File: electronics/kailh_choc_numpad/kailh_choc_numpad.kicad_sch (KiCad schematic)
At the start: 18 parts

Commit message: placed keycaps
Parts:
- cap16, cap17: footprint SquantorSwitches:KAILH_choc_keycap_2 -> SquantorSwitches:KAILH_choc_keycap_2_vertical
- cap5: footprint SquantorSwitches:KAILH_choc_keycap_2 -> SquantorSwitches:KAILH_choc_keycap_2_horizontal
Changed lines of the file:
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@@
       (effects (font (size 1.27 1.27)) (justify left))
     )
-    (property "Footprint" "SquantorSwitches:KAILH_choc_keycap_2" (id 2) (at 279.4 156.21 0)
+    (property "Footprint" "SquantorSwitches:KAILH_choc_keycap_2_vertical" (id 2) (at 279.4 156.21 0)
       (effects (font (size 1.27 1.27)) hide)
     )
@@
       (effects (font (size 1.27 1.27)) (justify left))
     )
-    (property "Footprint" "SquantorSwitches:KAILH_choc_keycap_2" (id 2) (at 264.16 156.21 0)
+    (property "Footprint" "SquantorSwitches:KAILH_choc_keycap_2_horizontal" (id 2) (at 264.16 156.21 0)
       (effects (font (size 1.27 1.27)) hide)
     )
@@
       (effects (font (size 1.27 1.27)) (justify left))
     )
-    (property "Footprint" "SquantorSwitches:KAILH_choc_keycap_2" (id 2) (at 279.4 146.05 0)
+    (property "Footprint" "SquantorSwitches:KAILH_choc_keycap_2_vertical" (id 2) (at 279.4 146.05 0)
       (effects (font (size 1.27 1.27)) hide)
     )
@@
     )
     (path "/46586f3f-ccb3-4688-bf96-26d8b317093e"
-      (reference "cap5") (unit 1) (value "0") (footprint "SquantorSwitches:KAILH_choc_keycap_2")
+      (reference "cap5") (unit 1) (value "0") (footprint "SquantorSwitches:KAILH_choc_keycap_2_horizontal")
     )
     (path "/a19b66d3-f406-4ce2-9e7f-6ceaff8d737f"
@@
     )
     (path "/7aa684ab-344d-440b-882a-86f99a2f3576"
-      (reference "cap16") (unit 1) (value "+") (footprint "SquantorSwitches:KAILH_choc_keycap_2")
+      (reference "cap16") (unit 1) (value "+") (footprint "SquantorSwitches:KAILH_choc_keycap_2_vertical")
     )
     (path "/2aef11e5-d526-4e94-8bfe-a0576a35db83"
-      (reference "cap17") (unit 1) (value "ent") (footprint "SquantorSwitches:KAILH_choc_keycap_2")
-    )
-  )
+      (reference "cap17") (unit 1) (value "ent") (footprint "SquantorSwitches:KAILH_choc_keycap_2_vertical")
+    )
+  )

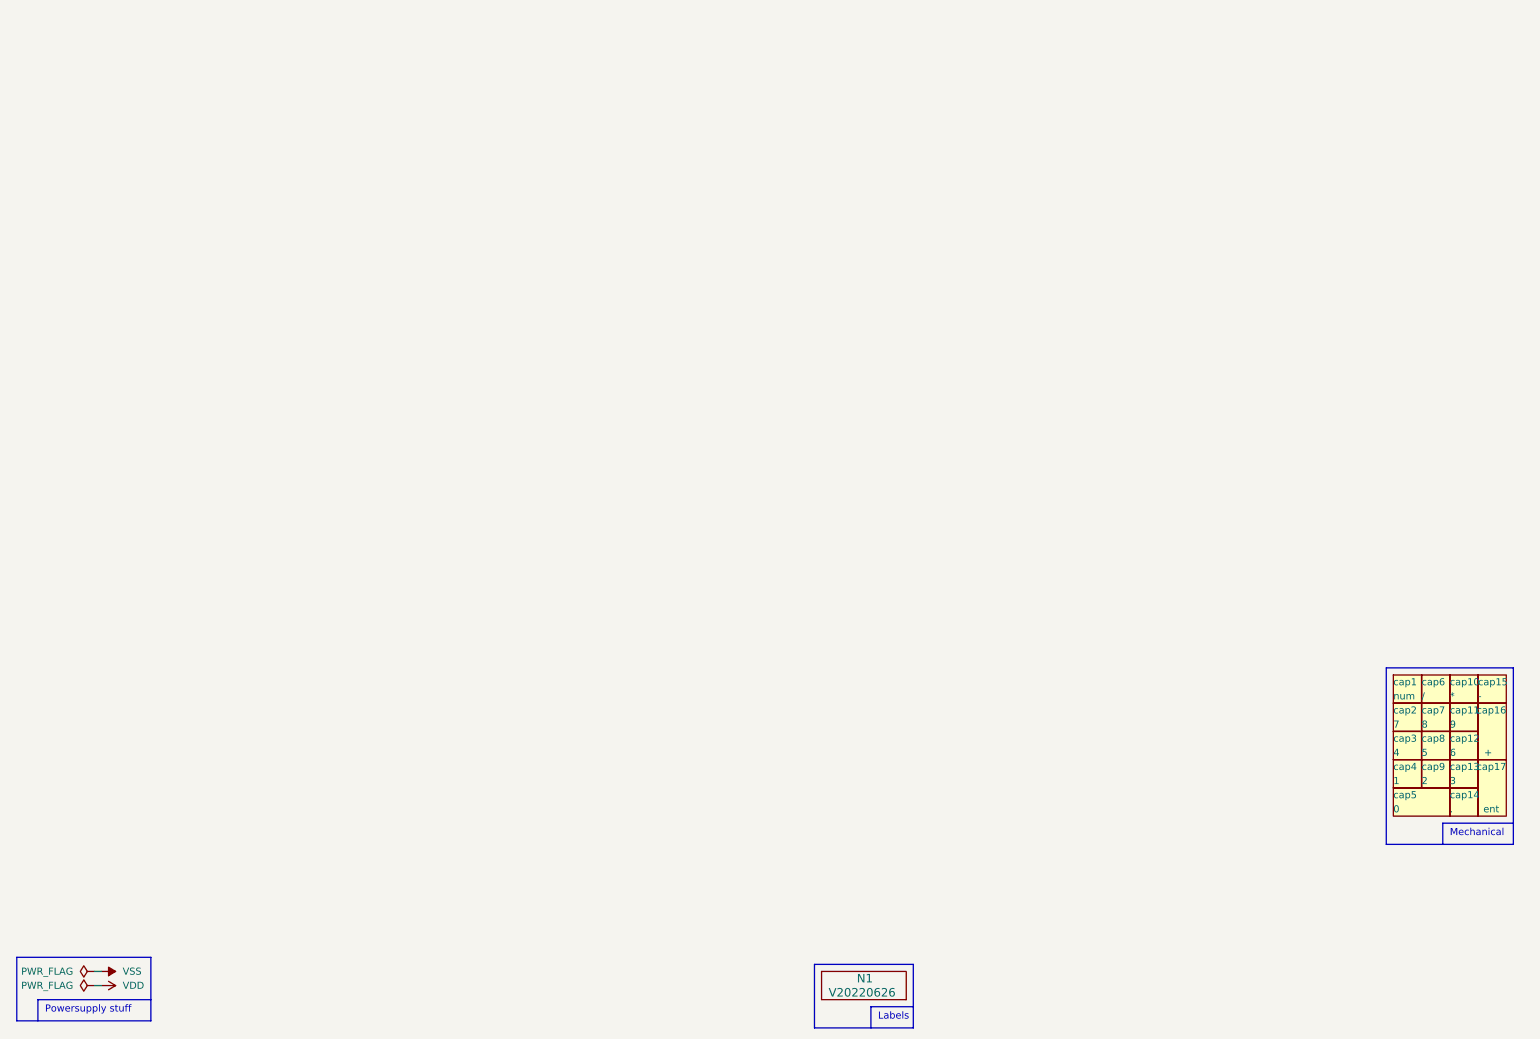
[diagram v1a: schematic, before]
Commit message: placing and routing keyboard matrix
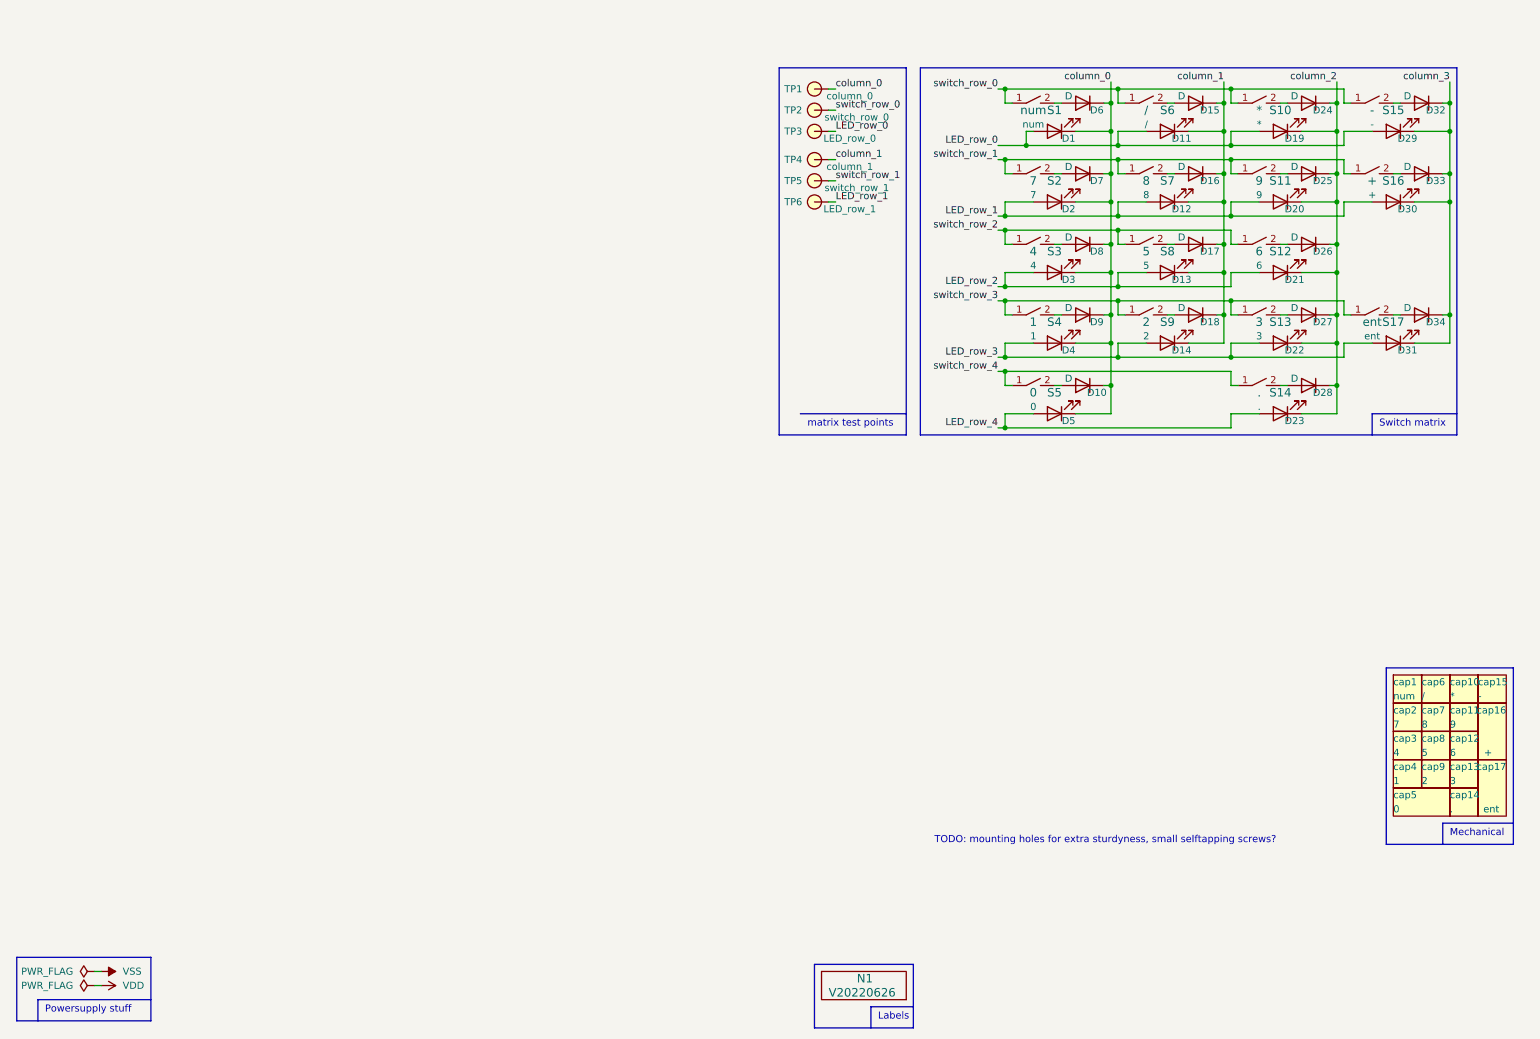
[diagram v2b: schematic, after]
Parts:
- added D1: num, SquantorDiodes:LED_1208_0603, symbol Device:LED
- added D10, D15, D16, D17, D18, D24, D25, D26, D27, D28, D32, D33, D34, D6, D7, D8, D9: D, SquantorDiodes:SOD-523_hand, symbol Device:D
- added D11: /, SquantorDiodes:LED_1208_0603, symbol Device:LED
- added D12: 8, SquantorDiodes:LED_1208_0603, symbol Device:LED
- added D13: 5, SquantorDiodes:LED_1208_0603, symbol Device:LED
- added D14: 2, SquantorDiodes:LED_1208_0603, symbol Device:LED
- added D19: *, SquantorDiodes:LED_1208_0603, symbol Device:LED
- added D2: 7, SquantorDiodes:LED_1208_0603, symbol Device:LED
- added D20: 9, SquantorDiodes:LED_1208_0603, symbol Device:LED
- added D21: 6, SquantorDiodes:LED_1208_0603, symbol Device:LED
- added D22: 3, SquantorDiodes:LED_1208_0603, symbol Device:LED
- added D23: ., SquantorDiodes:LED_1208_0603, symbol Device:LED
- added D29: -, SquantorDiodes:LED_1208_0603, symbol Device:LED
- added D3: 4, SquantorDiodes:LED_1208_0603, symbol Device:LED
- added D30: +, SquantorDiodes:LED_1208_0603, symbol Device:LED
- added D31: ent, SquantorDiodes:LED_1208_0603, symbol Device:LED
- added D4: 1, SquantorDiodes:LED_1208_0603, symbol Device:LED
- added D5: 0, SquantorDiodes:LED_1208_0603, symbol Device:LED
- added S1: num, SquantorSwitches:KAILH_choc_LED, symbol SquantorSwitches:2pin_tact_switch
- added S10: *, SquantorSwitches:KAILH_choc_LED, symbol SquantorSwitches:2pin_tact_switch
- added S11: 9, SquantorSwitches:KAILH_choc_LED, symbol SquantorSwitches:2pin_tact_switch
- added S12: 6, SquantorSwitches:KAILH_choc_LED, symbol SquantorSwitches:2pin_tact_switch
- added S13: 3, SquantorSwitches:KAILH_choc_LED, symbol SquantorSwitches:2pin_tact_switch
- added S14: ., SquantorSwitches:KAILH_choc_LED, symbol SquantorSwitches:2pin_tact_switch
- added S15: -, SquantorSwitches:KAILH_choc_LED, symbol SquantorSwitches:2pin_tact_switch
- added S16: +, SquantorSwitches:KAILH_choc_LED, symbol SquantorSwitches:2pin_tact_switch
- added S17: ent, SquantorSwitches:KAILH_choc_LED, symbol SquantorSwitches:2pin_tact_switch
- added S2: 7, SquantorSwitches:KAILH_choc_LED, symbol SquantorSwitches:2pin_tact_switch
- added S3: 4, SquantorSwitches:KAILH_choc_LED, symbol SquantorSwitches:2pin_tact_switch
- added S4: 1, SquantorSwitches:KAILH_choc_LED, symbol SquantorSwitches:2pin_tact_switch
- added S5: 0, SquantorSwitches:KAILH_choc_LED, symbol SquantorSwitches:2pin_tact_switch
- added S6: /, SquantorSwitches:KAILH_choc_LED, symbol SquantorSwitches:2pin_tact_switch
- added S7: 8, SquantorSwitches:KAILH_choc_LED, symbol SquantorSwitches:2pin_tact_switch
- added S8: 5, SquantorSwitches:KAILH_choc_LED, symbol SquantorSwitches:2pin_tact_switch
- added S9: 2, SquantorSwitches:KAILH_choc_LED, symbol SquantorSwitches:2pin_tact_switch
- added TP1: column_0, SquantorTestPoints:TestPoint_hole_H05R10, symbol SquantorProto:testpad
- added TP2: switch_row_0, SquantorTestPoints:TestPoint_hole_H05R10, symbol SquantorProto:testpad
- added TP3: LED_row_0, SquantorTestPoints:TestPoint_hole_H05R10, symbol SquantorProto:testpad
- added TP4: column_1, SquantorTestPoints:TestPoint_hole_H05R10, symbol SquantorProto:testpad
- added TP5: switch_row_1, SquantorTestPoints:TestPoint_hole_H05R10, symbol SquantorProto:testpad
- added TP6: LED_row_1, SquantorTestPoints:TestPoint_hole_H05R10, symbol SquantorProto:testpad
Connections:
- new net: D32.2 (A), S15.2
- new net: D24.2 (A), S10.2
- new net: D27.2 (A), S13.2
- new net: D7.2 (A), S2.2
- new net: D6.2 (A), S1.2
- new net: D9.2 (A), S4.2
- new net: D10.2 (A), S5.2
- new net: D26.2 (A), S12.2
- new net: D16.2 (A), S7.2
- new net: D25.2 (A), S11.2
- new net: D18.2 (A), S9.2
- new net: D8.2 (A), S3.2
- new net: D17.2 (A), S8.2
- new net: D28.2 (A), S14.2
- new net: D34.2 (A), S17.2
- new net: D15.2 (A), S6.2
- new net: D33.2 (A), S16.2
- new net LED_row_0: D1.2 (A), D11.2 (A), D19.2 (A), D29.2 (A), TP3.1
- new net LED_row_1: D12.2 (A), D2.2 (A), D20.2 (A), D30.2 (A), TP6.1
- new net LED_row_2: D13.2 (A), D21.2 (A), D3.2 (A)
- new net LED_row_3: D14.2 (A), D22.2 (A), D31.2 (A), D4.2 (A)
- new net LED_row_4: D23.2 (A), D5.2 (A)
- new net column_0: D1.1 (K), D10.1 (K), D2.1 (K), D3.1 (K), D4.1 (K), D5.1 (K), D6.1 (K), D7.1 (K), D8.1 (K), D9.1 (K), TP1.1
- new net column_1: D11.1 (K), D12.1 (K), D13.1 (K), D14.1 (K), D15.1 (K), D16.1 (K), D17.1 (K), D18.1 (K), TP4.1
- new net column_2: D19.1 (K), D20.1 (K), D21.1 (K), D22.1 (K), D23.1 (K), D24.1 (K), D25.1 (K), D26.1 (K), D27.1 (K), D28.1 (K)
- new net column_3: D29.1 (K), D30.1 (K), D31.1 (K), D32.1 (K), D33.1 (K), D34.1 (K)
- new net switch_row_0: S1.1, S10.1, S15.1, S6.1, TP2.1
- new net switch_row_1: S11.1, S16.1, S2.1, S7.1, TP5.1
- new net switch_row_2: S12.1, S3.1, S8.1
- new net switch_row_3: S13.1, S17.1, S4.1, S9.1
- new net switch_row_4: S14.1, S5.1
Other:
- note added: "Switch matrix"
- note added: "TODO: mounting holes for extra sturdyness, small selftapping screws?"
- note added: "matrix test points"

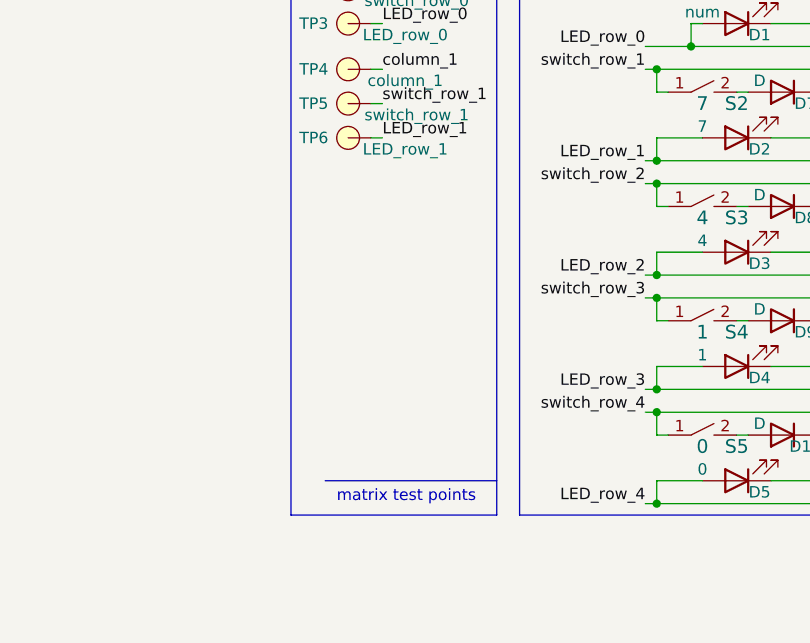
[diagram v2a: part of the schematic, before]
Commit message: fully placed and routed switch matrix
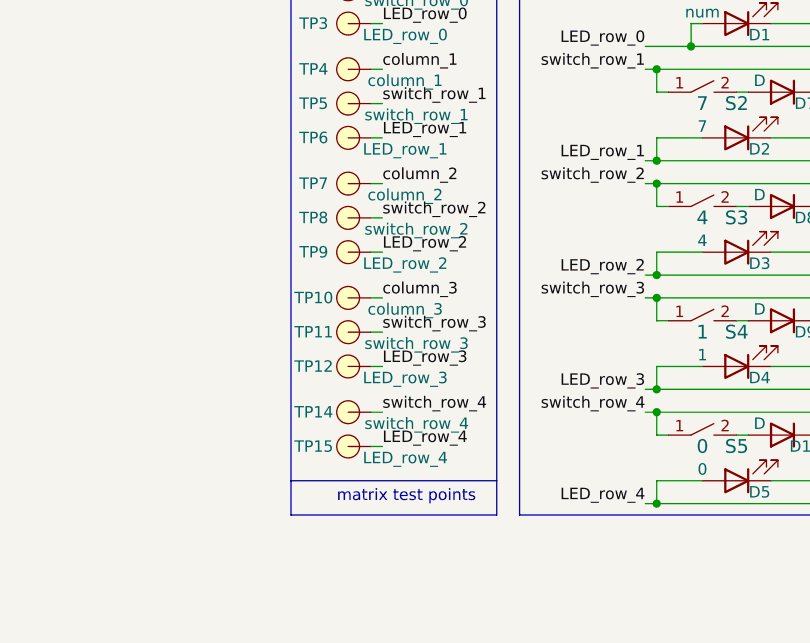
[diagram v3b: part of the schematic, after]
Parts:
- added TP10: column_3, SquantorTestPoints:TestPoint_hole_H05R10, symbol SquantorProto:testpad
- added TP11: switch_row_3, SquantorTestPoints:TestPoint_hole_H05R10, symbol SquantorProto:testpad
- added TP12: LED_row_3, SquantorTestPoints:TestPoint_hole_H05R10, symbol SquantorProto:testpad
- added TP14: switch_row_4, SquantorTestPoints:TestPoint_hole_H05R10, symbol SquantorProto:testpad
- added TP15: LED_row_4, SquantorTestPoints:TestPoint_hole_H05R10, symbol SquantorProto:testpad
- added TP7: column_2, SquantorTestPoints:TestPoint_hole_H05R10, symbol SquantorProto:testpad
- added TP8: switch_row_2, SquantorTestPoints:TestPoint_hole_H05R10, symbol SquantorProto:testpad
- added TP9: LED_row_2, SquantorTestPoints:TestPoint_hole_H05R10, symbol SquantorProto:testpad
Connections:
- net LED_row_2: now also TP9.1
- net LED_row_3: now also TP12.1
- net LED_row_4: now also TP15.1
- net column_2: now also TP7.1
- net column_3: now also TP10.1
- net switch_row_2: now also TP8.1
- net switch_row_3: now also TP11.1
- net switch_row_4: now also TP14.1
